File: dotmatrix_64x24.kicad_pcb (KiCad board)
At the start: 2 copper layers, 180 x 100 mm, 777 parts, among them CON1 BARREL_JACK, P1 CONN_01X09, P2 CONN_01X09, P3 CONN_01X04, P4 CONN_01X03, P5 USB_OTG, P6 CONN_01X03, Q1 NJL7302L-F3, Q2 Q_PNP_BEC 2SA1162, Q3 Q_NPN_BCE RN5006, SW1 SW_PUSH_SMALL_H, SW2 SW_PUSH_SMALL_H, SW3 SW_PUSH_SMALL_H, SW4 SW_PUSH_SMALL_H, SW5 SW_PUSH_SMALL_H, SW6 SW_PUSH_SMALL_H, SW7 SW_PUSH_SMALL_H, SW8 SW_PUSH_SMALL_H, U1 WROOM-02, U10 LED1642GW, U11 LED1642GW, U12 AE-BME280, U13 TPS54426, U14 NJU7223, U15 DS1307, U16 CH340G, U17 OSRB38C9AA, U18 BME280, U2 74HC595-alt-vdd, U3 TD62783, U4 74HC595-alt-vdd, U5 TD62783, U6 LED1642GW, U7 74HC595-alt-vdd, U8 TD62783, U9 LED1642GW, X1 CRYSTAL_SMD, Y1 12MHz

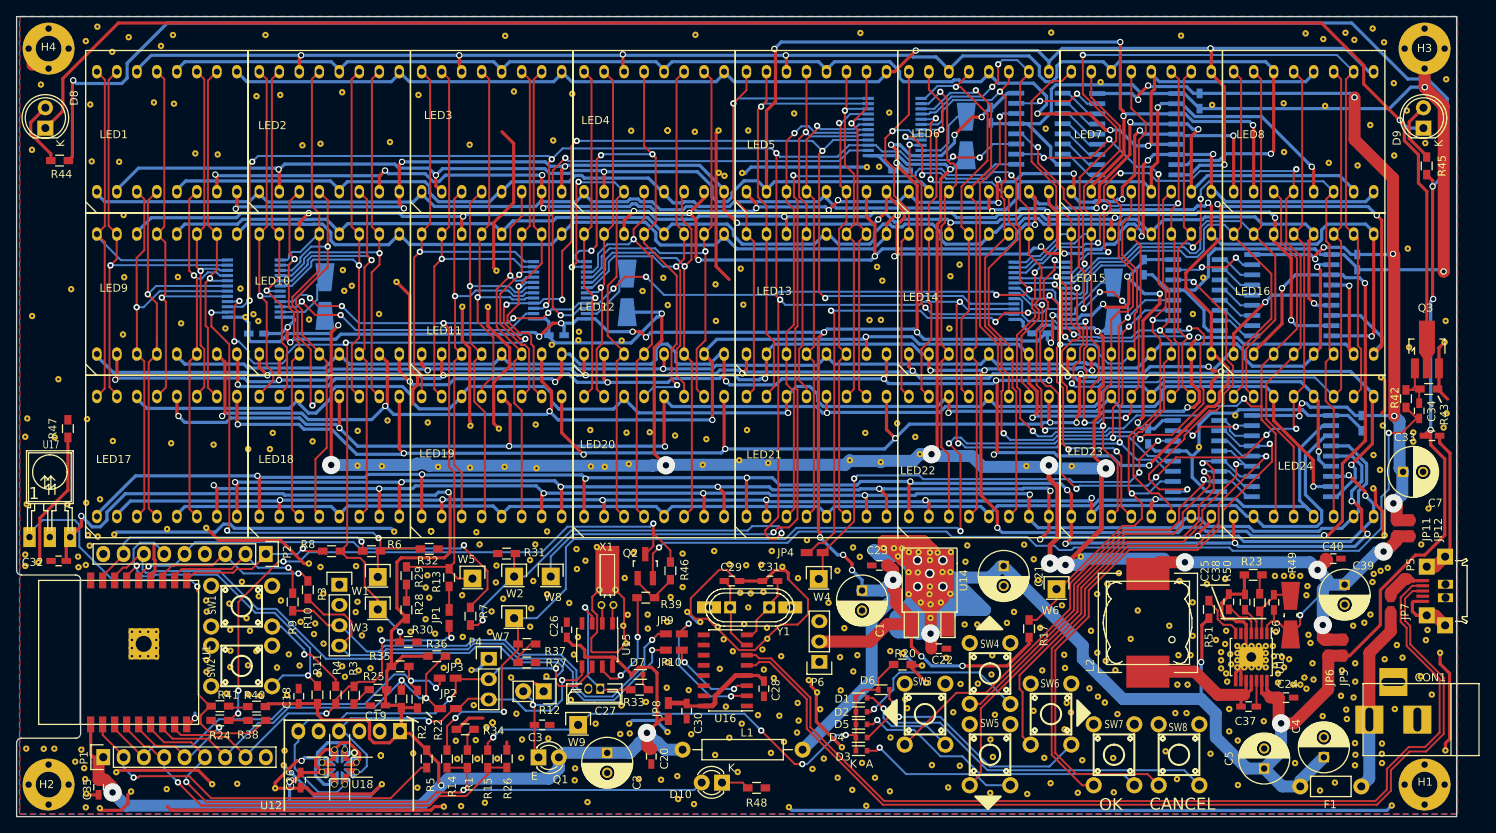
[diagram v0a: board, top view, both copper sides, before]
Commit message: Trace fixes
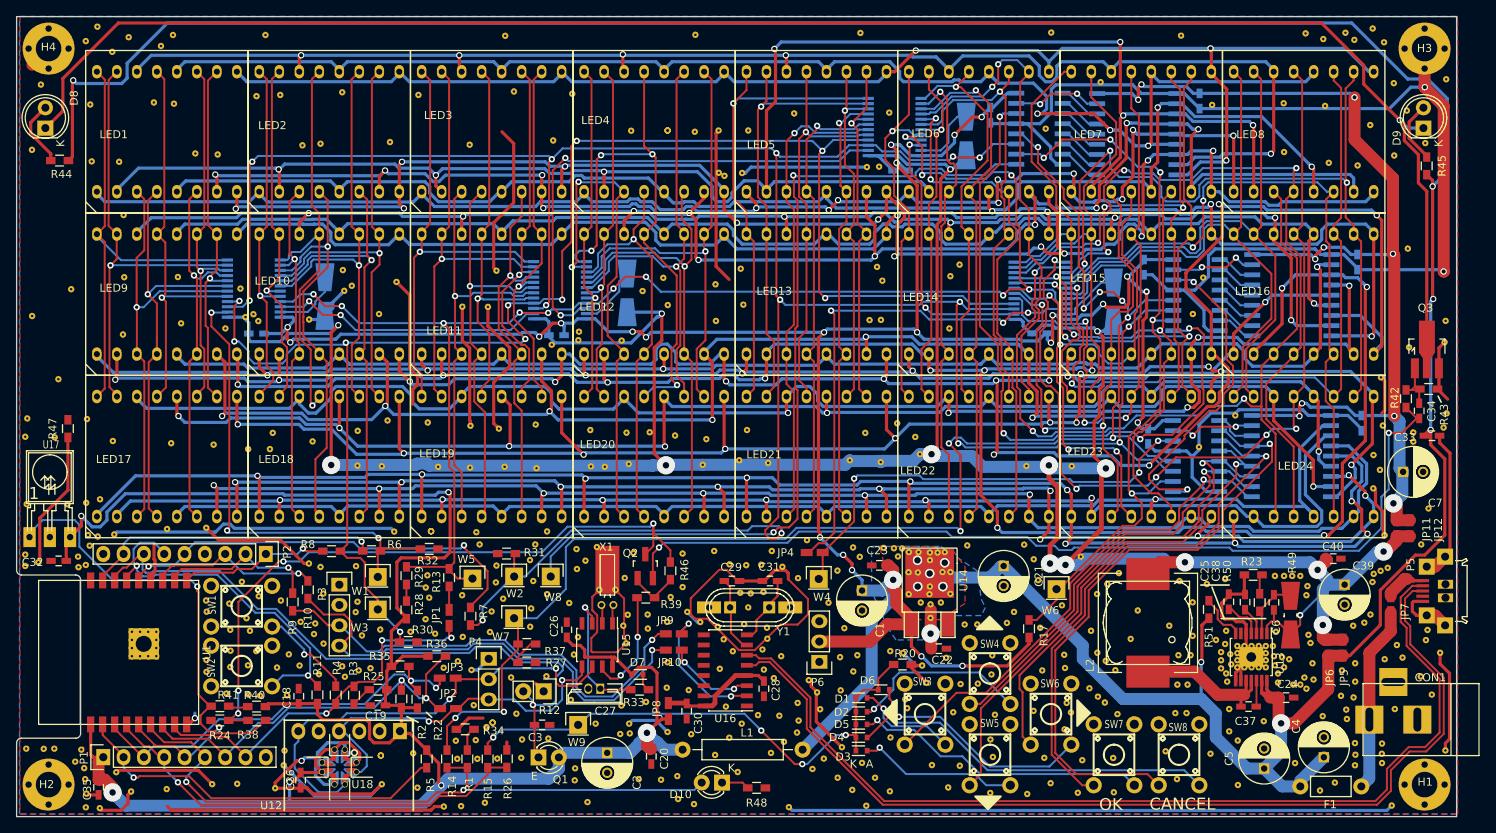
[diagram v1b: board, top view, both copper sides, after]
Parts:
- removed the REF** at (130.6, 80.1)
- moved REF** 0.76 mm to (128.0, 78.9)
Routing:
- net VCC: track 573.5 -> 385.0 mm
- net /Sheet57A04605/c60: track 110.0 -> 97.9 mm, vias 2 -> 3
- net GND: track 1068.9 -> 1075.2 mm
- net /LEDLOGICVDD: track 316.4 -> 314.2 mm
- net /Sheet57A04605/r6: track 199.2 -> 200.7 mm
- net /Sheet57A04605/c20: track 47.7 -> 46.4 mm
- net /Sheet57A04605/c54: track 68.5 -> 69.6 mm
- net /Sheet57A04605/COLLATCH: track 202.7 -> 201.8 mm
- net /Sheet57A04605/r3: track 199.5 -> 200.4 mm
- net /Sheet57A04605/c45: track 64.4 -> 63.6 mm
- net /Sheet57A04605/c46: track 56.7 -> 55.8 mm
- net /Sheet57A04605/c11: track 52.6 -> 51.8 mm
- net /Sheet57A04605/c9: track 52.8 -> 52.1 mm
- net /Sheet57A04605/c49: track 76.0 -> 75.3 mm
- net /Sheet57A04605/LEDVDD: track 131.1 -> 131.8 mm
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- added copper zone on B.Cu, net VCC
- added copper zone on F.Cu, net VCC

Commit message: Various fixes
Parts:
- removed the REF** at (42.4, 96.9)
- added REF**: stitch-via-0.6mm, components:stitch-via-0.8mm, F.Cu at (145.0, 20.2)
- added REF**: stitch-via-0.6mm, components:stitch-via-0.8mm, F.Cu at (78.5, 90.7)
- added REF**: stitch-via-0.6mm, components:stitch-via-0.8mm, F.Cu at (124.0, 105.5)
- added REF**: stitch-via-0.6mm, components:stitch-via-0.8mm, F.Cu at (115.7, 77.6)
- added REF**: stitch-via-0.6mm, components:stitch-via-0.8mm, F.Cu at (107.1, 25.9)
- added REF**: stitch-via-0.6mm, components:stitch-via-0.8mm, F.Cu at (111.9, 24.1)
- added REF**: stitch-via-0.6mm, components:stitch-via-0.8mm, F.Cu at (114.0, 24.1)
- added REF**: stitch-via-0.6mm, components:stitch-via-0.8mm, F.Cu at (123.6, 25.3)
- added REF**: stitch-via-0.6mm, components:stitch-via-0.8mm, F.Cu at (50.8, 96.6)
- added REF**: stitch-via-0.6mm, components:stitch-via-0.8mm, F.Cu at (48.4, 96.8)
- added REF**: stitch-via-0.6mm, components:stitch-via-0.8mm, F.Cu at (44.7, 98.6)
- added REF**: stitch-via-0.6mm, components:stitch-via-0.8mm, F.Cu at (45.5, 102.1)
- moved REF** 1.37 mm to (123.2, 79.8)
- moved REF** 1.07 mm to (40.9, 91.3)
- moved REF** 0.56 mm to (45.8, 96.3)
- moved REF** 0.52 mm to (58.1, 62.9)
- moved REF** 0.38 mm to (121.4, 78.7)
- moved REF** 0.33 mm to (120.4, 78.7)
- moved REF** 0.28 mm to (40.9, 88.8)
- moved REF** 0.13 mm to (38.6, 93.2)
- moved REF** 0.13 mm to (38.6, 91.3)
- moved REF** 0.10 mm to (38.6, 88.6)
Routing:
- net GND: track 1075.2 -> 1060.5 mm, vias 15 -> 16
- net /Sheet57A04605/r18: track 179.3 -> 173.1 mm
- net /Sheet57A04605/HC595LATCH: track 186.7 -> 182.3 mm
- net /Sheet57A04605/c44: track 62.0 -> 57.7 mm, vias 2 -> 1
- net /ESPVDD: track 290.0 -> 287.1 mm, vias 6 -> 8
- net /SDA: track 51.6 -> 48.9 mm
- net /Sheet57A04605/r24: track 166.8 -> 169.3 mm
- net /Sheet57A04605/r4: track 170.3 -> 172.6 mm
- net /Sheet57A04605/r1: track 173.8 -> 171.5 mm
- net Net-(P1-Pad5): track 15.1 -> 17.1 mm
- net /Sheet57A04605/c9: track 52.1 -> 50.3 mm
- net Net-(P1-Pad2): track 47.8 -> 49.6 mm
- net /LEDLOGICVDD: track 314.2 -> 312.7 mm
- net /Sheet57A04605/r21: track 213.3 -> 211.9 mm
- net /Sheet57A04605/HC595SER: track 60.8 -> 59.8 mm
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
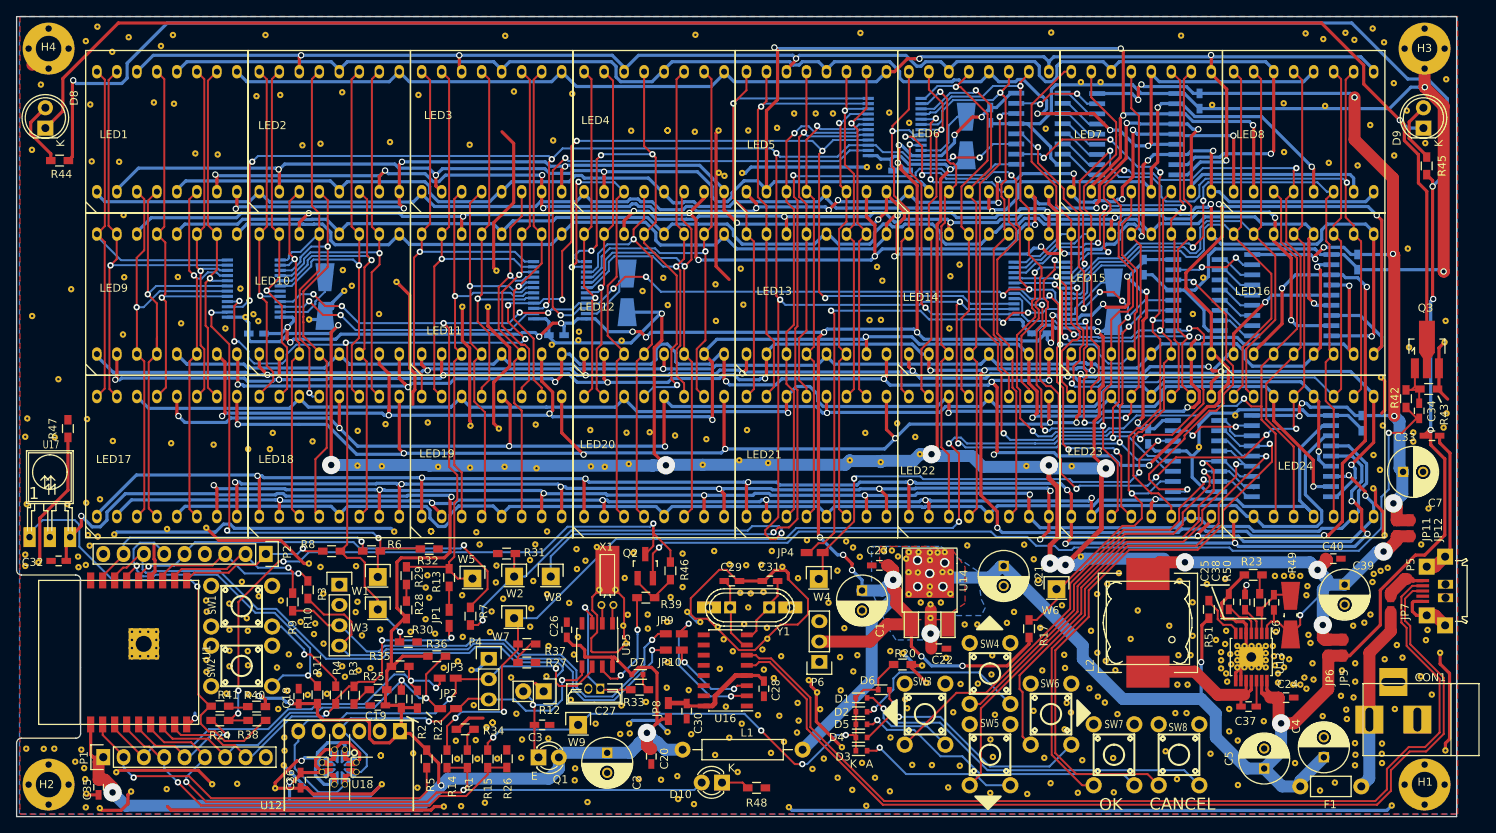
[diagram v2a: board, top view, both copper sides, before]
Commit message: To use COLSER signal as both IR input and column data signal output
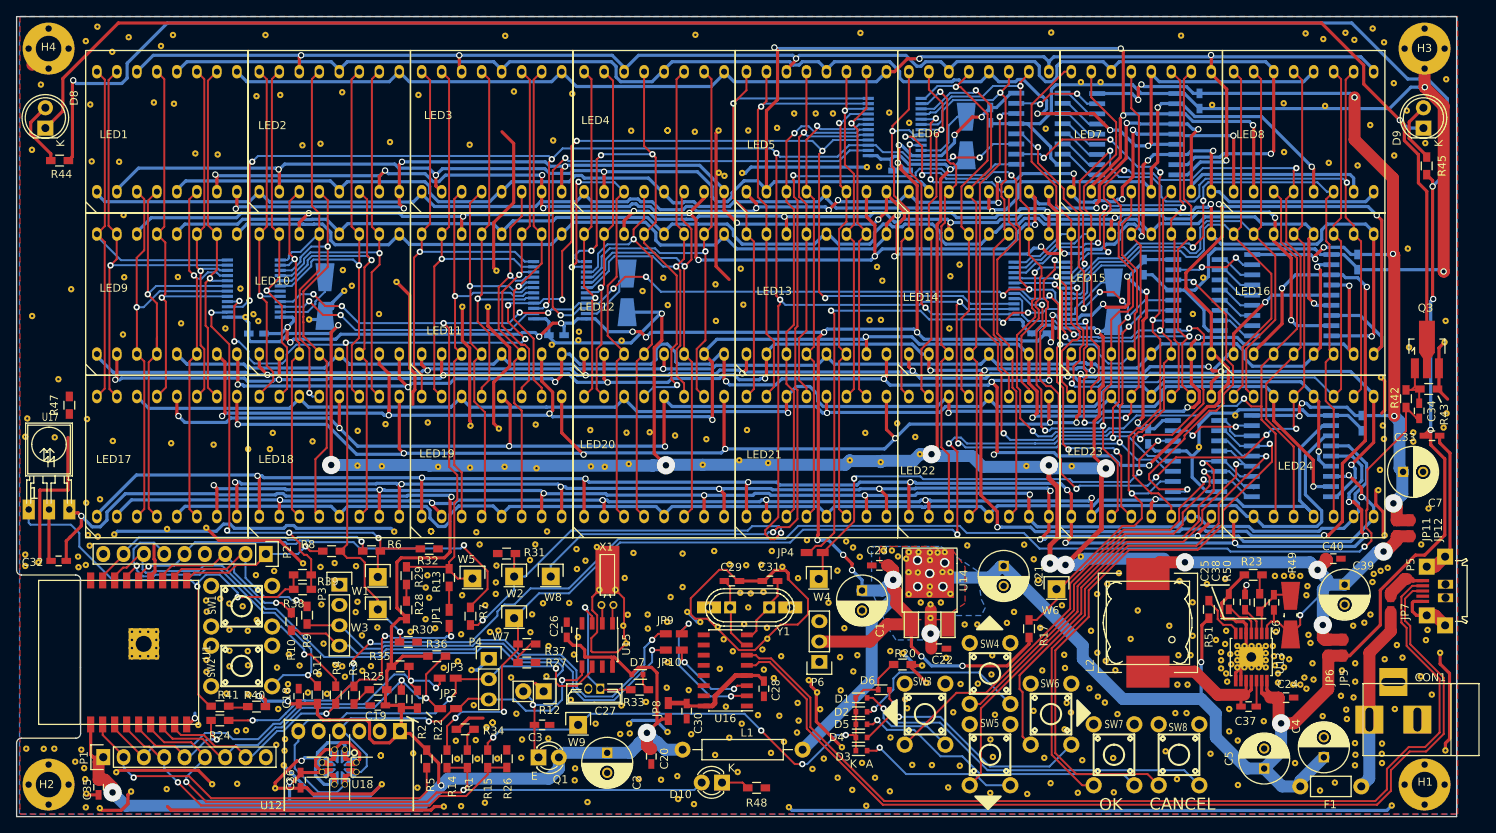
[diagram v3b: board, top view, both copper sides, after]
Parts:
- removed Q2: Q_PNP_BEC 2SA1162, TO_SOT_Packages_SMD:SOT-23_Handsoldering
- removed R46: 10k, Resistors_SMD:R_0603_HandSoldering
- removed the REF** at (76.3, 86.0)
- removed the REF** at (76.6, 82.5)
- removed the REF** at (40.2, 82.7)
- removed the REF** at (78.3, 84.2)
- removed the REF** at (72.8, 84.8)
- removed the REF** at (42.3, 84.5)
- removed the REF** at (49.2, 89.2)
- removed the REF** at (47.5, 87.7)
- removed the REF** at (49.3, 87.9)
- removed the REF** at (45.0, 85.0)
- removed the REF** at (50.3, 84.1)
- removed the REF** at (45.8, 96.3)
- removed the REF** at (18.4, 72.9)
- removed the REF** at (13.3, 72.9)
- removed the REF** at (71.4, 86.4)
- added REF**: stitch-via-0.6mm, components:stitch-via-0.8mm, F.Cu at (44.5, 103.0)
- added REF**: stitch-via-0.6mm, components:stitch-via-0.8mm, F.Cu at (72.2, 88.7)
- added REF**: stitch-via-0.6mm, components:stitch-via-0.8mm, F.Cu at (70.6, 85.6)
- added REF**: stitch-via-0.6mm, components:stitch-via-0.8mm, F.Cu at (71.9, 84.2)
- added REF**: stitch-via-0.6mm, components:stitch-via-0.8mm, F.Cu at (34.7, 100.5)
- added REF**: stitch-via-0.6mm, components:stitch-via-0.8mm, F.Cu at (40.3, 85.7)
- added REF**: stitch-via-0.6mm, components:stitch-via-0.8mm, F.Cu at (44.2, 81.3)
- added REF**: stitch-via-0.6mm, components:stitch-via-0.8mm, F.Cu at (41.9, 81.8)
- added REF**: stitch-via-0.6mm, components:stitch-via-0.8mm, F.Cu at (50.1, 85.5)
- added REF**: stitch-via-0.6mm, components:stitch-via-0.8mm, F.Cu at (51.8, 80.3)
- added REF**: stitch-via-0.6mm, components:stitch-via-0.8mm, F.Cu at (40.7, 101.2)
- added REF**: stitch-via-0.6mm, components:stitch-via-0.8mm, F.Cu at (39.5, 101.3)
- added REF**: stitch-via-0.6mm, components:stitch-via-0.8mm, F.Cu at (51.8, 93.0)
- added REF**: stitch-via-0.6mm, components:stitch-via-0.8mm, F.Cu at (45.8, 96.3)
- added REF**: stitch-via-0.6mm, components:stitch-via-0.8mm, F.Cu at (45.9, 95.4)
- added REF**: stitch-via-0.6mm, components:stitch-via-0.8mm, F.Cu at (37.5, 84.8)
- added REF**: stitch-via-0.6mm, components:stitch-via-0.8mm, F.Cu at (76.2, 89.0)
- added REF**: stitch-via-0.6mm, components:stitch-via-0.8mm, F.Cu at (77.8, 85.3)
- R32: value 10k -> 10k DNI
- R39: value 1k -> 10k
- moved R39 43.0 mm to (47.7, 81.8)
- moved R38 17.4 mm to (47.7, 83.6)
- moved R10 4.47 mm to (46.3, 87.6)
- moved U17 3.46 mm to (16.1, 73.6)
- moved R47 2.93 mm to (18.6, 60.6)
- moved R9 2.45 mm to (48.3, 86.8)
- moved REF** 2.40 mm to (182.9, 64.8)
- moved REF** 1.57 mm to (76.4, 86.7)
- moved REF** 1.27 mm to (42.0, 87.4)
- moved REF** 0.74 mm to (47.8, 80.3)
- moved REF** 0.67 mm to (182.2, 71.2)
- moved REF** 0.67 mm to (64.3, 88.5)
- moved REF** 0.46 mm to (55.2, 93.8)
- moved REF** 0.44 mm to (57.1, 88.4)
- moved REF** 0.39 mm to (67.6, 89.2)
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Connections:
- C34 pad 2: Net-(C34-Pad2) -> /IR_OUT
- R24 pad 1: /IR -> /IR_OUT
- R38 pad 1: /IR -> /IR_IN
- R38 pad 2: Net-(R38-Pad2) -> /Sheet57A04605/COLSER
- R39 pad 1: /IR_Sensor_RTC/#IR_LED_EN -> /IR_IN
- R39 pad 2: Net-(Q2-Pad1) -> /Sheet57A04605/COLSER
- R41 pad 2: Net-(R38-Pad2) -> /IR_IN
- R42 pad 1: Net-(C34-Pad2) -> /IR_OUT
- U15 pad 7: /IR_Sensor_RTC/#IR_LED_EN -> Net-(U15-Pad7)
- U17 pad 1: Net-(R38-Pad2) -> /IR_IN
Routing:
- net /IR_OUT: track 0.00 -> 178.7 mm, vias 0 -> 4
- net Net-(C34-Pad2): track 116.8 -> 0.00 mm, vias 2 -> 0
- net /IR: track 83.8 -> 0.00 mm, vias 4 -> 0
- net /IR_IN: track 0.00 -> 59.4 mm, vias 0 -> 2
- net Net-(R38-Pad2): track 56.2 -> 0.00 mm, vias 1 -> 0
- net /IR_Sensor_RTC/#IR_LED_EN: track 14.0 -> 0.00 mm, vias 2 -> 0
- net /Sheet57A04605/COLSER: track 60.2 -> 68.6 mm, vias 3 -> 4
- net GND: track 1060.5 -> 1068.8 mm
- net Net-(Q2-Pad1): track 6.49 -> 0.00 mm
- net /TXD: track 59.9 -> 56.3 mm
- net /RXD: track 58.2 -> 55.5 mm
- net Net-(P2-Pad2): track 20.1 -> 22.7 mm
- net /ESPVDD: track 287.1 -> 289.0 mm
- net Net-(P1-Pad5): track 17.1 -> 15.5 mm
- net /Sheet57A04605/HC595LATCH: track 182.3 -> 183.5 mm
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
